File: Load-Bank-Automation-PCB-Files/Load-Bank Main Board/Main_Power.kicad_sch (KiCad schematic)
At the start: 22 parts, among them J2 USB_C_Receptacle_USB2.0_14P, J3 Barrel_Jack_MountingPin, U3 USBLC6-2SC6, U7 AZ1117IH-5.0, U8 AZ1117IH-3.3

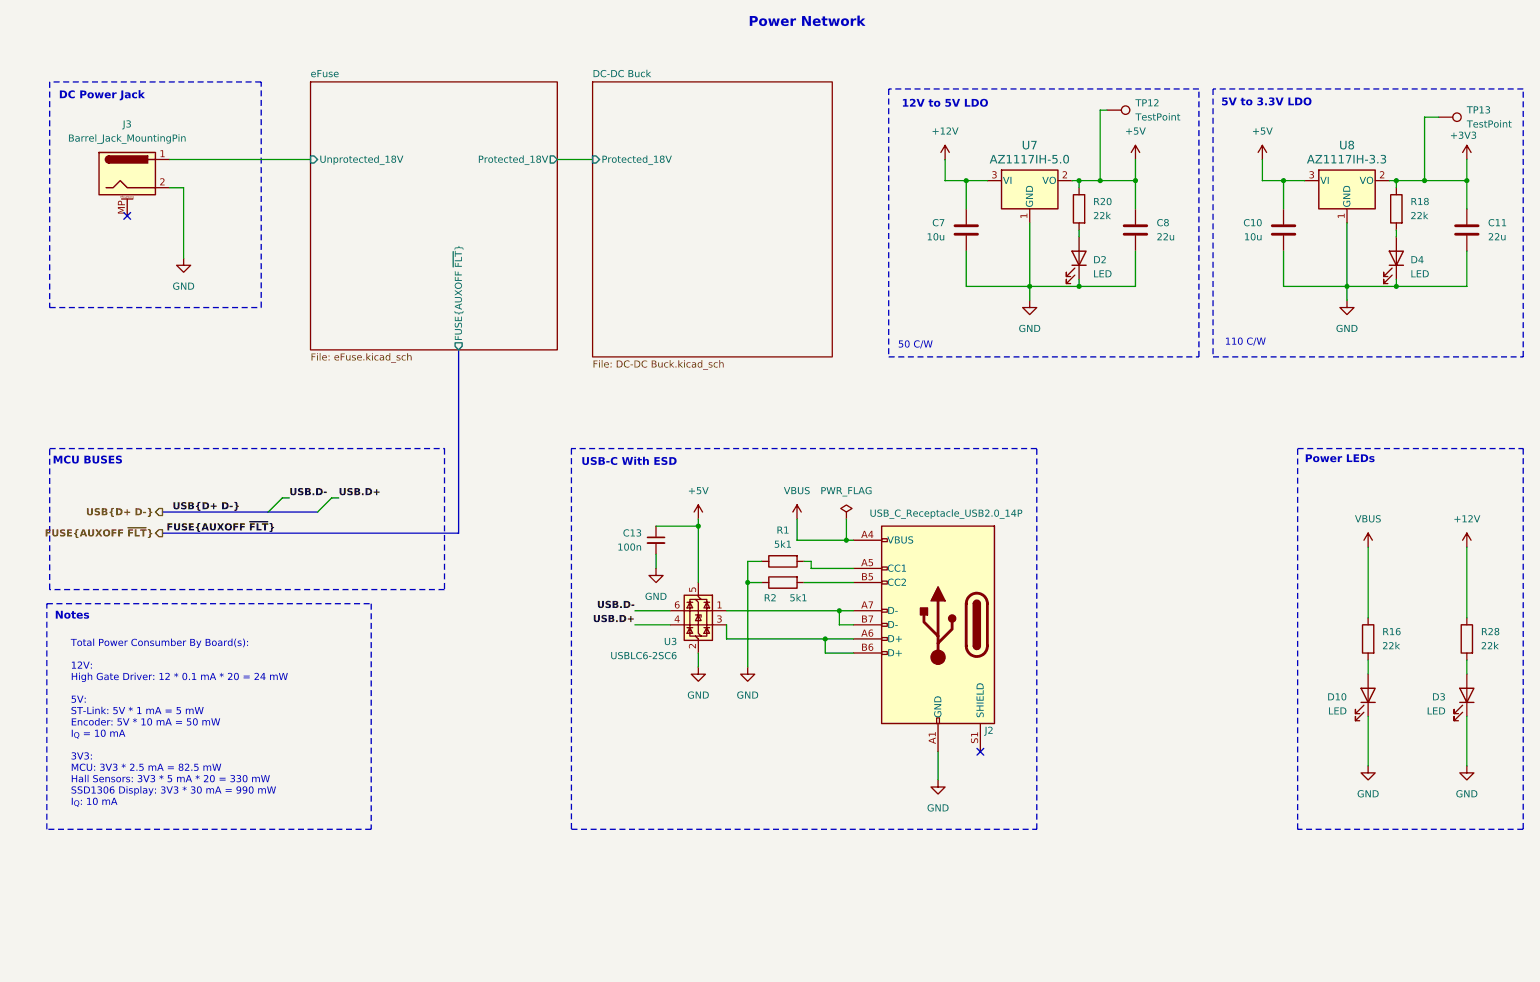
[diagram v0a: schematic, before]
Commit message: Replaced 12V-5V LDO with buck
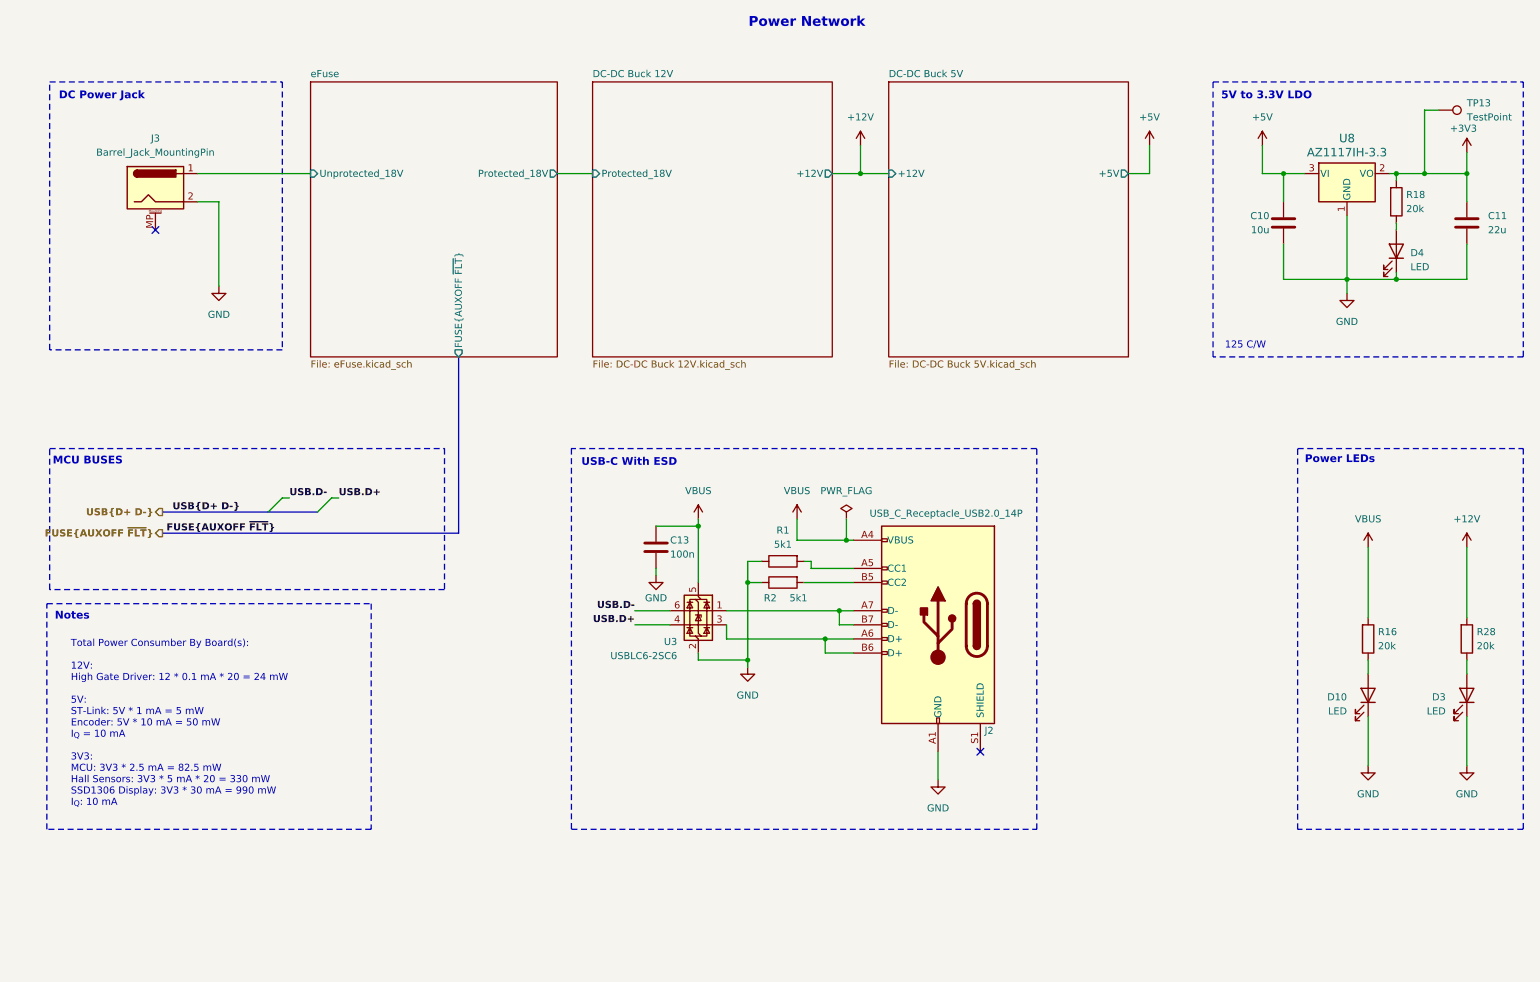
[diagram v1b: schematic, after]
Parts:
- removed C13: 100n, Capacitor_SMD:C_1206_3216Metric_Pad1.33x1.80mm_HandSolder, symbol Device:C_Small
- removed C7: 10u, Capacitor_SMD:C_1206_3216Metric_Pad1.33x1.80mm_HandSolder, symbol Device:C
- removed C8: 22u, Capacitor_SMD:C_0805_2012Metric_Pad1.18x1.45mm_HandSolder, symbol Device:C
- removed D2: LED, LED_SMD:LED_0603_1608Metric, symbol Device:LED
- removed R20: 22k, Resistor_SMD:R_1206_3216Metric_Pad1.30x1.75mm_HandSolder, symbol Device:R
- removed TP12: TestPoint, TestPoint:TestPoint_Pad_D1.5mm, symbol Connector:TestPoint
- removed U7: AZ1117IH-5.0, Package_TO_SOT_SMD:SOT-223-3_TabPin2, symbol EcoCar_Library:AZ1117IH-5.0
- added C13: 100n, Capacitor_SMD:C_1206_3216Metric_Pad1.33x1.80mm_HandSolder, symbol Device:C
- R16, R18, R28: value 22k -> 20k; footprint Resistor_SMD:R_1206_3216Metric_Pad1.30x1.75mm_HandSolder -> Resistor_SMD:R_0603_1608Metric_Pad0.98x0.95mm_HandSolder
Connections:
- net +12V: now also R28.2; no longer R28.1
- net +3V3: now also R18.2; no longer R18.1
- net +5V: no longer U3.5 (VBUS)
- net GND: now also C13.2
- net VBUS: now also R16.2, U3.5 (VBUS), C13.1; no longer R16.1
- net at D4.2 (A): now also R18.1; no longer R18.2
- net at D10.2 (A): now also R16.1; no longer R16.2
- net at D3.2 (A): now also R28.1; no longer R28.2
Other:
- sheet DC-DC Buck renamed DC-DC Buck 12V
- added sheet DC-DC Buck 5V (DC-DC Buck 5V.kicad_sch)
- sheet DC-DC Buck 12V: file DC-DC Buck.kicad_sch -> DC-DC Buck 12V.kicad_sch
- sheet DC-DC Buck 12V ports: added +12V; removed none
- note added: "125 C/W"
- note removed: "110 C/W"
- note removed: "12V to 5V LDO"
- note removed: "50 C/W"
- moved on the sheet: C11, D4, J3, TP13, U8

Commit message: Commit
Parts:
- added U7: AZ1117IH-3.3, Package_TO_SOT_SMD:SOT-223-3_TabPin2, symbol EcoCar_Library:AZ1117IH-3.3
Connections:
- net +3V3: now also U7.2 (VO)
- net +5V: now also U7.3 (VI)
- net GND: now also U7.1 (GND)
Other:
- moved on the sheet: C10, C11, D10, D3, D4, R16, R18, R28, TP13, U8

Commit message: A
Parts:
- removed TP13: TestPoint, TestPoint:TestPoint_Pad_D1.5mm, symbol Connector:TestPoint
- C13: footprint Capacitor_SMD:C_1206_3216Metric_Pad1.33x1.80mm_HandSolder -> Capacitor_SMD:C_0603_1608Metric_Pad1.08x0.95mm_HandSolder
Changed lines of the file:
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@@
-	)
-	(junction
-		(at 255.27 48.26)
-		(diameter 0)
-		(color 0 0 0 0)
 	)
 	(junction
@@
 	(wire
 		(pts
-			(xy 252.73 48.26) (xy 255.27 48.26)
+			(xy 252.73 48.26) (xy 262.89 48.26)
 		)
 		(stroke
@@
 	(wire
 		(pts
-			(xy 255.27 48.26) (xy 262.89 48.26)
-		)
-		(stroke
-			(width 0)
-			(type default)
-		)
-	)
-	(wire
-		(pts
 			(xy 158.75 105.41) (xy 158.75 109.22)
 		)
@@
 	(wire
 		(pts
-			(xy 255.27 40.64) (xy 255.27 48.26)
-		)
-		(stroke
-			(width 0)
-			(type default)
-		)
-	)
-	(wire
-		(pts
 			(xy 149.86 104.14) (xy 149.86 109.22)
 		)
@@
 		(pts
 			(xy 266.7 43.18) (xy 266.7 48.26)
-		)
-		(stroke
-			(width 0)
-			(type default)
-		)
-	)
-	(wire
-		(pts
-			(xy 257.81 40.64) (xy 255.27 40.64)
 		)
 		(stroke
@@
 	)
 	(symbol
-		(lib_id "Device:C")
-		(at 124.46 110.49 0)
-		(unit 1)
-		(exclude_from_sim no)
-		(in_bom yes)
-		(on_board yes)
-		(dnp no)
-		(property "Reference" "C13"
-			(at 127 109.22 0)
-			(effects
-				(font
-					(size 1.27 1.27)
-				)
-				(justify left)
-			)
-		)
-		(property "Value" "100n"
-			(at 127 111.76 0)
-			(effects
-				(font
-					(size 1.27 1.27)
-				)
-				(justify left)
-			)
-		)
-		(property "Footprint" "Capacitor_SMD:C_1206_3216Metric_Pad1.33x1.80mm_HandSolder"
-			(at 125.4252 114.3 0)
-			(effects
-				(font
-					(size 1.27 1.27)
-				)
-				(hide yes)
-			)
-		)
-		(property "Datasheet" "Capacitor_SMD:C_0805_2012Metric_Pad1.18x1.45mm_HandSolder"
-			(at 124.46 110.49 0)
-			(effects
-				(font
-					(size 1.27 1.27)
-				)
-				(hide yes)
-			)
-		)
-		(property "Description" "Unpolarized capacitor"
-			(at 124.46 110.49 0)
-			(effects
-				(font
-					(size 1.27 1.27)
-				)
-				(hide yes)
-			)
-		)
-		(pin "1"
-		)
-		(pin "2"
-		)
-		(instances
-			(project "Main Board"
-				(path "/c82c4769-33eb-46b7-8d07-39045014a3da/eb9b9647-818b-4f6a-aec9-7481a1a3b43c"
-					(reference "C13")
-					(unit 1)
-				)
-			)
-		)
-	)
-	(symbol
 		(lib_id "Device:LED")
 		(at 262.89 137.16 270)
@@
 	)
 	(symbol
-		(lib_id "Connector:TestPoint")
-		(at 257.81 40.64 270)
-		(unit 1)
-		(exclude_from_sim no)
-		(in_bom yes)
-		(on_board yes)
-		(dnp no)
-		(property "Reference" "TP13"
-			(at 253.746 36.322 90)
-			(effects
-				(font
-					(size 1.27 1.27)
-				)
-				(justify left)
-			)
-		)
-		(property "Value" "TestPoint"
-			(at 253.492 38.862 90)
-			(effects
-				(font
-					(size 1.27 1.27)
-				)
-				(justify left)
-			)
-		)
-		(property "Footprint" "TestPoint:TestPoint_Pad_D1.5mm"
-			(at 257.81 45.72 0)
-			(effects
-				(font
-					(size 1.27 1.27)
-				)
-				(hide yes)
-			)
-		)
-		(property "Datasheet" "~"
-			(at 257.81 45.72 0)
-			(effects
-				(font
-					(size 1.27 1.27)
-				)
-				(hide yes)
-			)
-		)
-		(property "Description" "test point"
-			(at 257.81 40.64 0)
-			(effects
-				(font
-					(size 1.27 1.27)
-				)
-				(hide yes)
-			)
-		)
-		(pin "1"
-		)
-		(instances
-			(project "Main Board"
-				(path "/c82c4769-33eb-46b7-8d07-39045014a3da/eb9b9647-818b-4f6a-aec9-7481a1a3b43c"
-					(reference "TP13")
-					(unit 1)
-				)
-			)
-		)
-	)
-	(symbol
 		(lib_id "Device:R")
 		(at 262.89 127 0)
@@
 					(unit 1)
 				)
+			)
+		)
+	)
+	(symbol
+		(lib_id "Device:C")
+		(at 124.46 110.49 0)
+		(unit 1)
+		(exclude_from_sim no)
+		(in_bom yes)
+		(on_board yes)
+		(dnp no)
+		(property "Reference" "C13"
+			(at 127 109.22 0)
+			(effects
+				(font
+					(size 1.27 1.27)
+				)
+				(justify left)
+			)
+		)
+		(property "Value" "100n"
+			(at 127 111.76 0)
+			(effects
+				(font
+					(size 1.27 1.27)
+				)
+				(justify left)
+			)
+		)
+		(property "Footprint" "Capacitor_SMD:C_0603_1608Metric_Pad1.08x0.95mm_HandSolder"
+			(at 125.4252 114.3 0)
+			(effects
+				(font
+					(size 1.27 1.27)
+				)
+				(hide yes)
+			)
+		)
+		(property "Datasheet" ""
+			(at 124.46 110.49 0)
+			(effects
+				(font
+					(size 1.27 1.27)
+				)
+				(hide yes)
+			)
+		)
+		(property "Description" "Unpolarized capacitor"
+			(at 124.46 110.49 0)
+			(effects
+				(font
+					(size 1.27 1.27)
+				)
+				(hide yes)
+			)
+		)
+		(pin "1"
+		)
+		(pin "2"
+		)
+		(instances
+			(project "Main Board"
+				(path "/c82c4769-33eb-46b7-8d07-39045014a3da/eb9b9647-818b-4f6a-aec9-7481a1a3b43c"
+					(reference "C13")
+					(unit 1)
+				)

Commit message: A
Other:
- sheet eFuse ports: added none; removed FUSE{AUXOFF ~{FLT}}

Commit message: A
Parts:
- added C25: 10u, Capacitor_SMD:C_1206_3216Metric_Pad1.33x1.80mm_HandSolder, symbol Device:C
- added C26: 22u, Capacitor_SMD:C_0805_2012Metric_Pad1.18x1.45mm_HandSolder, symbol Device:C
- added D9: LED, LED_SMD:LED_0603_1608Metric, symbol Device:LED
- added R34: 20k, Resistor_SMD:R_0603_1608Metric_Pad0.98x0.95mm_HandSolder, symbol Device:R
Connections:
- net +3V3: now also C26.1, R34.2
- net +5V: now also C25.1
- net GND: now also C25.2, C26.2, D9.1 (K)
- new net: D9.2 (A), R34.1
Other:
- moved on the sheet: C10, C11, C13, D10, D3, D4, J2, J3, R1, R16, R18, R2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

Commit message: A
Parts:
- removed C10, C25: 10u, Capacitor_SMD:C_1206_3216Metric_Pad1.33x1.80mm_HandSolder, symbol Device:C
- removed C11, C26: 22u, Capacitor_SMD:C_0805_2012Metric_Pad1.18x1.45mm_HandSolder, symbol Device:C
- removed D4, D9: LED, LED_SMD:LED_0603_1608Metric, symbol Device:LED
- removed R18, R34: 20k, Resistor_SMD:R_0603_1608Metric_Pad0.98x0.95mm_HandSolder, symbol Device:R
- removed U7, U8: AZ1117IH-3.3, Package_TO_SOT_SMD:SOT-223-3_TabPin2, symbol EcoCar_Library:AZ1117IH-3.3
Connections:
- net eFuse/Unprotected_18V renamed eFuse/Unprotected_19V
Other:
- added sheet LDOs (5V - 3V3) (LDOs (5V - 3V3).kicad_sch)
- sheet DC-DC Buck 12V ports: added Protected_19V; removed Protected_18V
- sheet eFuse ports: added Protected_19V, Unprotected_19V; removed Protected_18V, Unprotected_18V
- note added: "Total Power Consumber By Board(s) (worst case): 3V3: MCU: 3V3 * 150 mA * 1 = 395 mW Hall Sensors: 3V3 * 5.5 mA * 20 = 363 mW SSD1306 Display: 3V3 * 30 mA * 1 = 99 mW I_{losses}: 3V3 * 100 mA * 1 = 330 mW P_{total} = 1287 mW 5V: ST-Link: 5V * 10 mA * 1 = 50 mW Encoder: 5V * 10 mA * 1 = 50 mW I_{losses}: 5V * 40 mA * 1 = 200 mW P_{total} = 300 mW 12V: High Gate Driver: 12V * 5 mA * 20 = 1200 mW I_{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"
- note removed: "125 C/W"
- note removed: "5V to 3.3V LDO"
- note removed: "Total Power Consumber By Board(s): 12V: High Gate Driver: 12 * 0.1 mA * 20 = 24 mW 5V: ST-Link: 5V * 1 mA = 5 mW Encoder: 5V * 10 mA = 50 mW I_{Q} = 10 mA 3V3: MCU: 3V3 * 2.5 mA = 82.5 mW Hall Sensors: 3V3 * 5 mA * 20 = 330 mW SSD1306 Display: 3V3 * 30 mA = 990 mW I_{Q}: 10 mA"
- moved on the sheet: C13, D10, D3, J2, R1, R16, R2, R28, U3

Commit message: Schematic Complete: New/Better Bucks
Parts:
- J3: footprint Connector_BarrelJack:BarrelJack_GCT_DCJ200-10-A_Horizontal -> Connector_BarrelJack:BarrelJack_TENSILITY_54-00130_Horizontal; Actual Wall Adapter https://www.amazon.ca/Security-01-Adapter-5-5x2-1mm-100mA-1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 -> (none); Digikey (none) -> https://www.digikey.ca/en/products/detail/tensility-interna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
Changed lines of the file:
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@@
 			)
 		)
-		(property "Footprint" "Connector_BarrelJack:BarrelJack_GCT_DCJ200-10-A_Horizontal"
+		(property "Footprint" "Connector_BarrelJack:BarrelJack_TENSILITY_54-00130_Horizontal"
 			(at 35.56 44.196 0)
 			(effects
@@
 			)
 		)
-		(property "Datasheet" "https://tensility.s3.us-west-2.amazonaws.com/uploads/pdffiles/54-00166.pdf"
+		(property "Datasheet" "https://tensility.s3.us-west-2.amazonaws.com/uploads/pdffiles/54-00130.pdf"
 			(at 35.56 44.196 0)
 			(effects
@@
 			)
 		)
-		(property "Actual Wall Adapter" "https://www.amazon.ca/Security-01-Adapter-5-5x2-1mm-100mA-1000mA-Equipment/dp/B09JVXSCCN/ref=sr_1_5?crid=AZLTDRD7S8GB&dib=eyJ2IjoiMSJ9.FGvEPvFDDSt6wc4Y85t0LcvG8AeOATC4grKpYQq-HhoB6JEEMt0MnNRb1S33KuBu_Qz1JDVarHNjFmkPBEKm6PE9z6pu30oK9U3AwlbPw6Bar2Nw5xDcnYqp7E1ISlM0qo8m0aEi2useDaQEmxFXGzl1czgjGwlu8PP4VCyFeVPDLIct1nd2AGsPslmuOrHhuqhPF-slu2fOycFee0mUtsGA1pMZku5X2b8JUtMXEtUVW1oWBJk8HIcrErOXXdDi83xJE-5565_OX5heTYNqk2IpVgvFAsJspzWD6wWXd84.XaeUdyik1OxtJVv26NURHl421ZvH8ZDXdN8-aas1XDU&dib_tag=se&keywords=dc%2Bbarrel%2Bconnector%2B18V&qid=1763326019&sprefix=dc%2Bbarrel%2Bconnector%2B18v%2Caps%2C176&sr=8-5&th=1"
+		(property "Digikey" "https://www.digikey.ca/en/products/detail/tensility-international-corp/54-00130/9685439"
 			(at 34.29 43.18 0)
 			(effects
@@
 			)
 		)
-		(property "Datasheet" ""
+		(property "Datasheet" "https://www.digikey.ca/en/products/detail/tdk-corporation/CGA3E2X7R1H104K080AA/2443144?s=N4IgTCBcDaIDoBcAEBhA4gQQMwFEwA0B2AJQEYAJUgBgBYBpKgDiowxAF0BfIA"
 			(at 109.22 101.6 0)
 			(effects
